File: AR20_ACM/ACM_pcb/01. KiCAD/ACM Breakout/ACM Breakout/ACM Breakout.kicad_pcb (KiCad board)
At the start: 2 copper layers, 30.5 x 44.5 mm, 3 parts, among them J1 Conn_01x15_Male, J2 Conn_01x15_Male, U1 ACM_2020

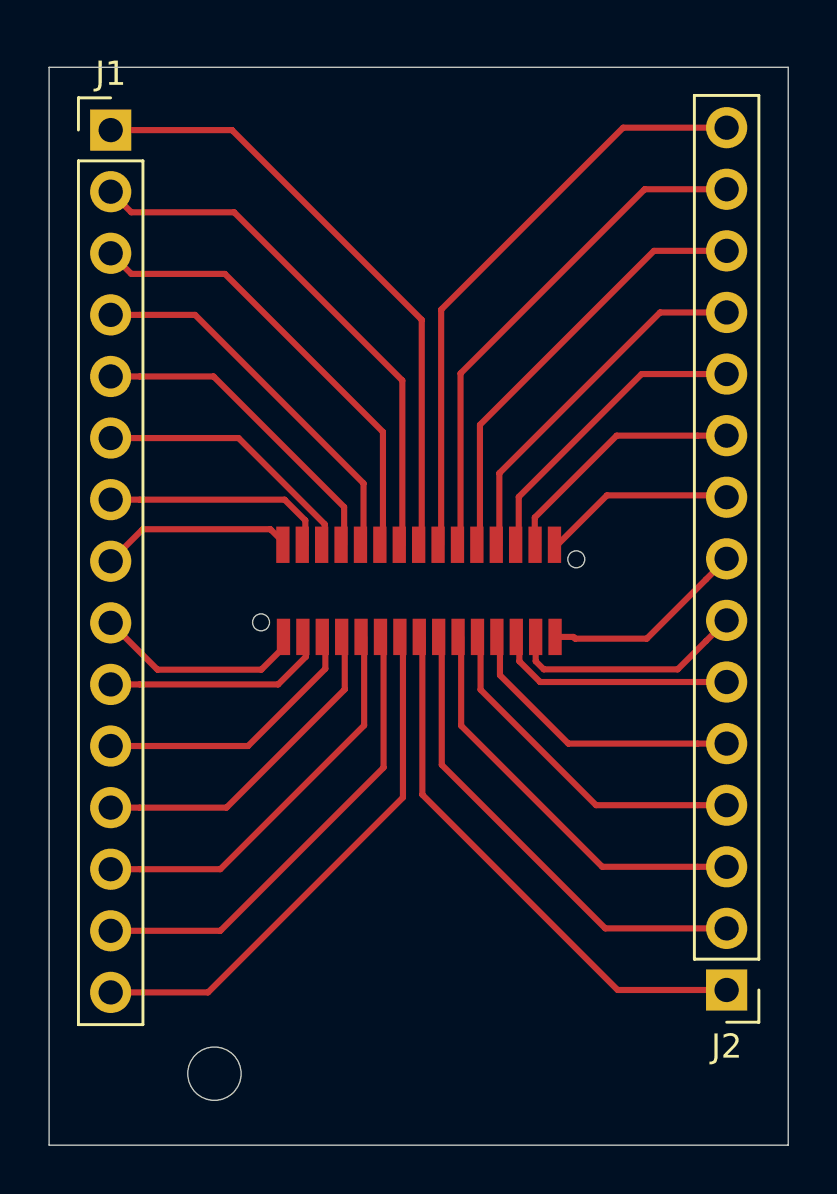
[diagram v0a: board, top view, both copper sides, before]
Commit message: Added namings to the ports
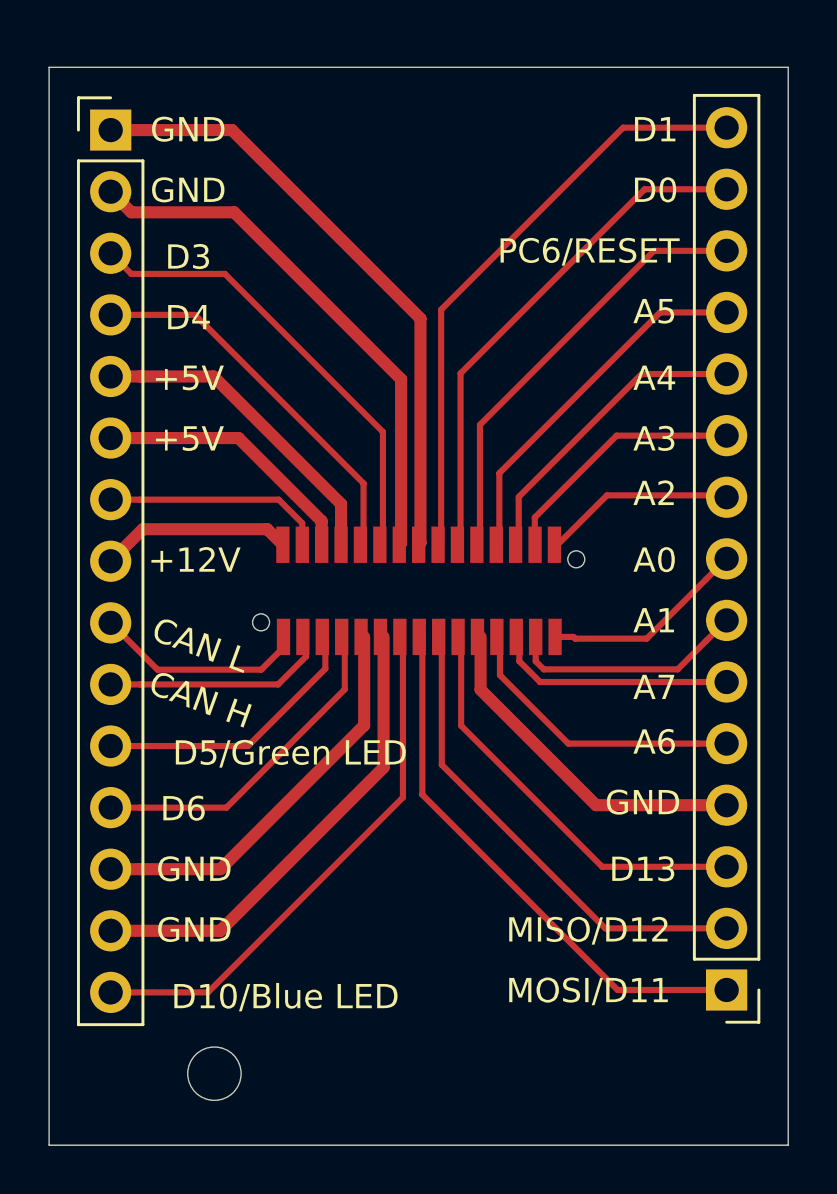
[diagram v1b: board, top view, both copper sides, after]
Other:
- board text added: "+12V"
- board text added: "+5V"
- board text added: "A0"
- board text added: "A1"
- board text added: "A2"
- board text added: "A3"
- board text added: "A4"
- board text added: "A5"
- board text added: "A6"
- board text added: "A7"
- board text added: "CAN H"
- board text added: "CAN L"
- board text added: "D0"
- board text added: "D1"
- board text added: "D10/Blue LED"
- board text added: "D13"
- board text added: "D3"
- board text added: "D4"
- board text added: "D5/Green LED"
- board text added: "D6"
- board text added: "GND"
- board text added: "MISO/D12"
- board text added: "MOSI/D11"
- board text added: "PC6/RESET"
